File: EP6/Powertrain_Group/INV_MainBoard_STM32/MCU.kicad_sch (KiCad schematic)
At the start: 56 parts, among them J4 STDC14, SW1 RESET, U22 TCAN1042VDRQ1, U4 STM32G474RETx, U5 CAT24C256, U6 TCAN1042VDRQ1, Y1 Crystal_GND23

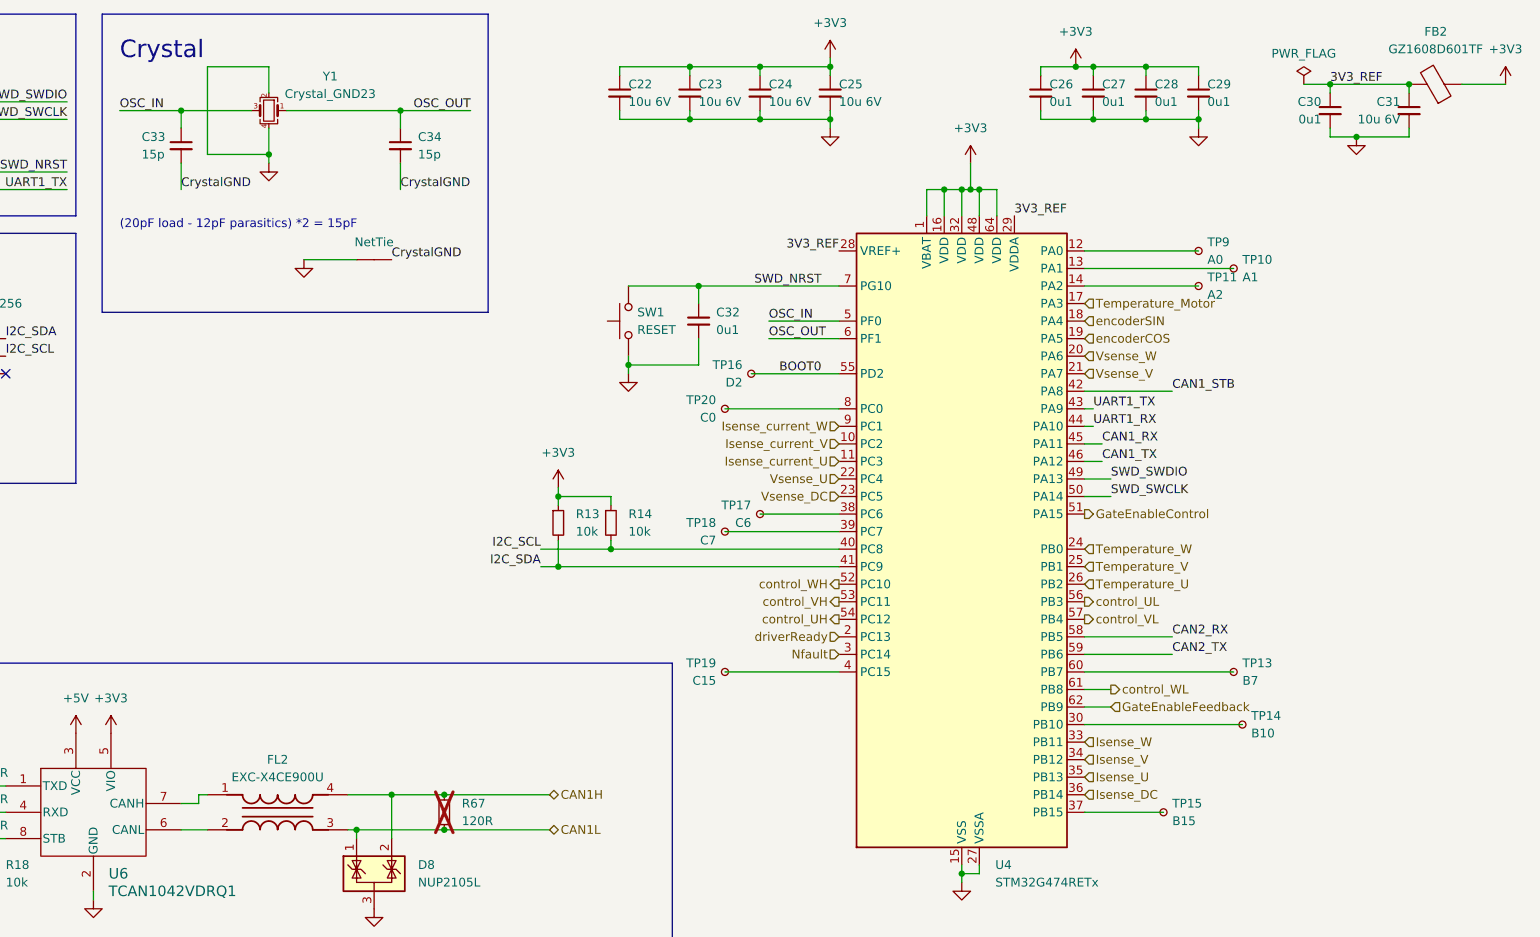
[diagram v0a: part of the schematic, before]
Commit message: batch update for JLCPCB 241117
6SBMS
ACC_HVLV1
INV_CurrentSense2
INV_CurrentSense3
DClinkCap1
INV_MainBoard_STM32
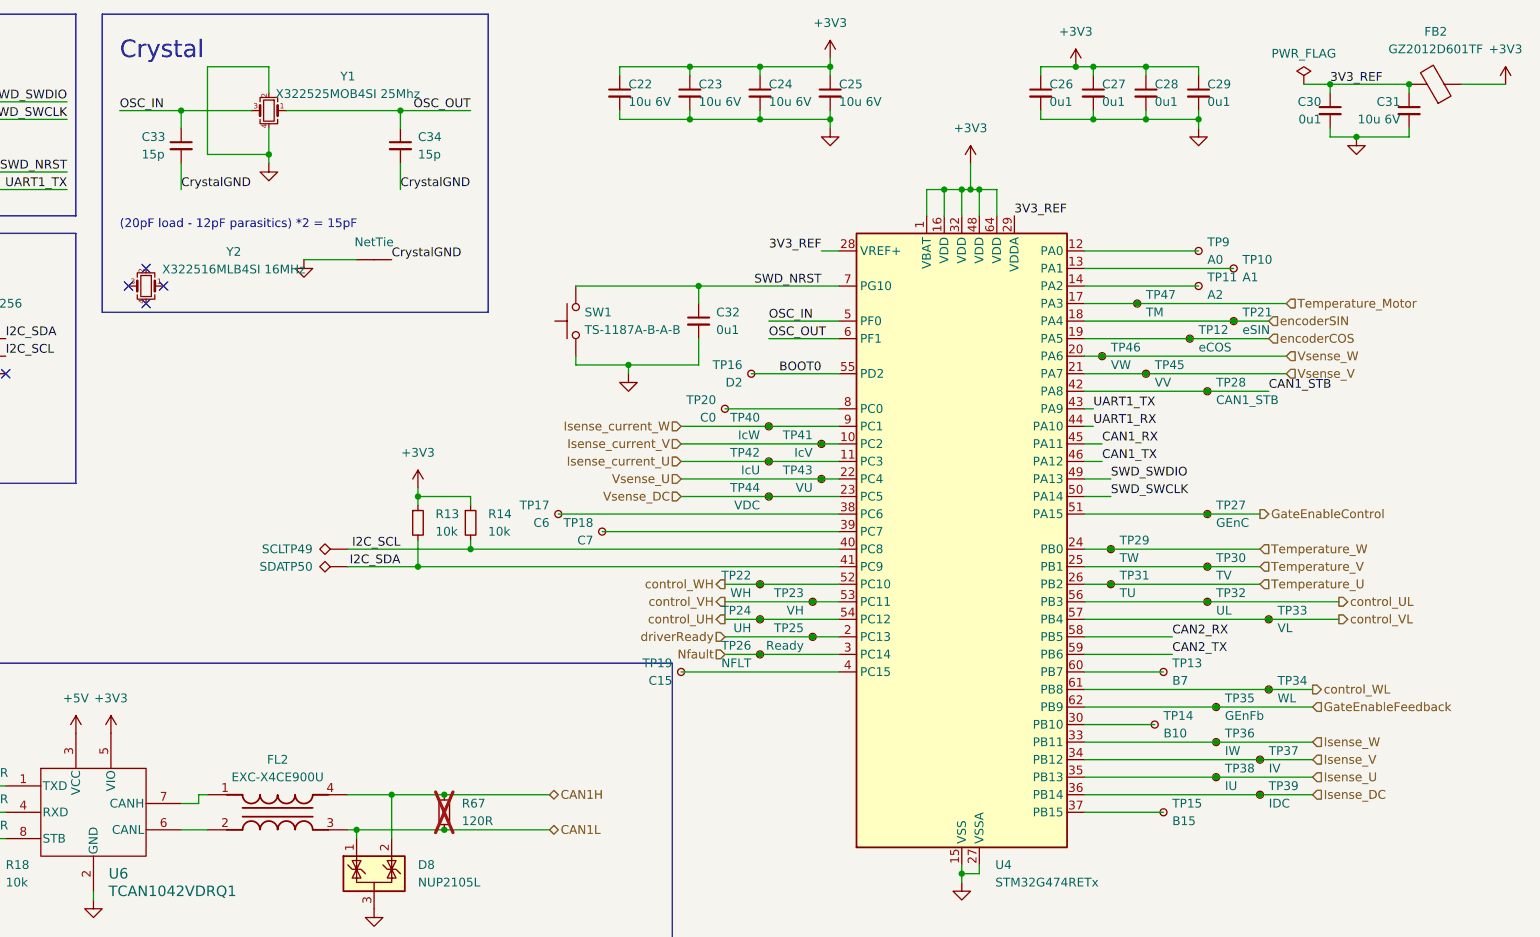
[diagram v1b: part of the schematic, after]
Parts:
- added TP12: eCOS, TestPoint:TestPoint_Pad_D1.0mm, symbol Connector:TestPoint_Small
- added TP21: eSIN, TestPoint:TestPoint_Pad_D1.0mm, symbol Connector:TestPoint_Small
- added TP22: WH, TestPoint:TestPoint_Pad_D1.0mm, symbol Connector:TestPoint_Small
- added TP23: VH, TestPoint:TestPoint_Pad_D1.0mm, symbol Connector:TestPoint_Small
- added TP24: UH, TestPoint:TestPoint_Pad_D1.0mm, symbol Connector:TestPoint_Small
- added TP25: Ready, TestPoint:TestPoint_Pad_D1.0mm, symbol Connector:TestPoint_Small
- added TP26: NFLT, TestPoint:TestPoint_Pad_D1.0mm, symbol Connector:TestPoint_Small
- added TP27: GEnC, TestPoint:TestPoint_Pad_D1.0mm, symbol Connector:TestPoint_Small
- added TP28: CAN1_STB, TestPoint:TestPoint_Pad_D1.0mm, symbol Connector:TestPoint_Small
- added TP29: TW, TestPoint:TestPoint_Pad_D1.0mm, symbol Connector:TestPoint_Small
- added TP30: TV, TestPoint:TestPoint_Pad_D1.0mm, symbol Connector:TestPoint_Small
- added TP31: TU, TestPoint:TestPoint_Pad_D1.0mm, symbol Connector:TestPoint_Small
- added TP32: UL, TestPoint:TestPoint_Pad_D1.0mm, symbol Connector:TestPoint_Small
- added TP33: VL, TestPoint:TestPoint_Pad_D1.0mm, symbol Connector:TestPoint_Small
- added TP34: WL, TestPoint:TestPoint_Pad_D1.0mm, symbol Connector:TestPoint_Small
- added TP35: GEnFb, TestPoint:TestPoint_Pad_D1.0mm, symbol Connector:TestPoint_Small
- added TP36: IW, TestPoint:TestPoint_Pad_D1.0mm, symbol Connector:TestPoint_Small
- added TP37: IV, TestPoint:TestPoint_Pad_D1.0mm, symbol Connector:TestPoint_Small
- added TP38: IU, TestPoint:TestPoint_Pad_D1.0mm, symbol Connector:TestPoint_Small
- added TP39: IDC, TestPoint:TestPoint_Pad_D1.0mm, symbol Connector:TestPoint_Small
- added TP40: IcW, TestPoint:TestPoint_Pad_D1.0mm, symbol Connector:TestPoint_Small
- added TP41: IcV, TestPoint:TestPoint_Pad_D1.0mm, symbol Connector:TestPoint_Small
- added TP42: IcU, TestPoint:TestPoint_Pad_D1.0mm, symbol Connector:TestPoint_Small
- added TP43: VU, TestPoint:TestPoint_Pad_D1.0mm, symbol Connector:TestPoint_Small
- added TP44: VDC, TestPoint:TestPoint_Pad_D1.0mm, symbol Connector:TestPoint_Small
- added TP45: VV, TestPoint:TestPoint_Pad_D1.0mm, symbol Connector:TestPoint_Small
- added TP46: VW, TestPoint:TestPoint_Pad_D1.0mm, symbol Connector:TestPoint_Small
- added TP47: TM, TestPoint:TestPoint_Pad_D1.0mm, symbol Connector:TestPoint_Small
- added TP49: SCL, TestPoint:TestPoint_THTPad_D1.0mm_Drill0.5mm, symbol Connector:TestPoint_Alt
- added TP50: SDA, TestPoint:TestPoint_THTPad_D1.0mm_Drill0.5mm, symbol Connector:TestPoint_Alt
- added Y2: X322516MLB4SI 16MHz, Crystal:Crystal_SMD_3225-4Pin_3.2x2.5mm, symbol Device:Crystal_GND24_Small
- FB2: value GZ1608D601TF -> GZ2012D601TF
- SW1: value RESET -> TS-1187A-B-A-B
- Y1: value Crystal_GND23 -> X322525MOB4SI 25Mhz
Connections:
- net CAN1_STB: now also TP28.1
- net GateEnableControl: now also TP27.1
- net GateEnableFeedback: now also TP35.1
- net I2C_SCL: now also TP49.1
- net I2C_SDA: now also TP50.1
- net Isense_DC: now also TP39.1
- net Isense_U: now also TP38.1
- net Isense_V: now also TP37.1
- net Isense_W: now also TP36.1
- net Isense_current_U: now also TP42.1
- net Isense_current_V: now also TP41.1
- net Isense_current_W: now also TP40.1
- net Nfault: now also TP26.1
- net Temperature_Motor: now also TP47.1
- net Temperature_U: now also TP31.1
- net Temperature_V: now also TP30.1
- net Temperature_W: now also TP29.1
- net Vsense_DC: now also TP44.1
- net Vsense_U: now also TP43.1
- net Vsense_V: now also TP45.1
- net Vsense_W: now also TP46.1
- net control_UH: now also TP24.1
- net control_UL: now also TP32.1
- net control_VH: now also TP23.1
- net control_VL: now also TP33.1
- net control_WH: now also TP22.1
- net control_WL: now also TP34.1
- net driverReady: now also TP25.1
- net encoderCOS: now also TP12.1
- net encoderSIN: now also TP21.1
- no-connect marks 9 -> 13
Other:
- moved on the sheet: R13, R14, SW1, TP13, TP14, TP17, TP18, TP19

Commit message: update INV_MainBoard_STM32 to V2.0
big update to match new INV_GateDriver
and use H743ZI as MCU
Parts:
- removed C18, C19, C36, C37: 0u1, Capacitor_SMD:C_0402_1005Metric, symbol Device:C_Small
- removed C35: 1u, Capacitor_SMD:C_0402_1005Metric, symbol Device:C_Small
- removed D17, D8: NUP2105L, Package_TO_SOT_SMD:SOT-23, symbol Power_Protection:NUP2105L
- removed FL2, FL3: EXC-X4CE900U, SamacSys_Parts_EP6:EXCX4CE900U, symbol SamacSys_Parts_EP6:EXC-X4CE900U
- removed J4: STDC14, nturt_kicad_lib_EP6:box_header_14P_pitch127, symbol Connector_Generic:Conn_02x07_Odd_Even
- removed JP1: CAN2STB, Jumper:SolderJumper-2_P1.3mm_Open_RoundedPad1.0x1.5mm, symbol Jumper:SolderJumper_2_Open
- removed R12: 100R, Resistor_SMD:R_0603_1608Metric, symbol Device:R_Small
- removed R15, R16, R17, R70, R71, R73: 100R, Resistor_SMD:R_0402_1005Metric, symbol Device:R_Small
- removed R67, R72: 120R, Resistor_SMD:R_0402_1005Metric, symbol Device:R_Small
- removed R74: 10k, Resistor_SMD:R_0402_1005Metric, symbol Device:R_Small
- removed TIE2: NetTie, NetTie:NetTie-2_SMD_Pad0.5mm, symbol PCM_4ms_Net-tie:NetTie
- removed TP10: A1, TestPoint:TestPoint_Pad_D1.0mm, symbol Connector:TestPoint_Small
- removed TP11: A2, TestPoint:TestPoint_Pad_D1.0mm, symbol Connector:TestPoint_Small
- removed TP12: eCOS, TestPoint:TestPoint_Pad_D1.0mm, symbol Connector:TestPoint_Small
- removed TP13: B7, TestPoint:TestPoint_Pad_D1.0mm, symbol Connector:TestPoint_Small
- removed TP14: B10, TestPoint:TestPoint_Pad_D1.0mm, symbol Connector:TestPoint_Small
- removed TP15: B15, TestPoint:TestPoint_Pad_D1.0mm, symbol Connector:TestPoint_Small
- removed TP16: D2, TestPoint:TestPoint_Pad_D1.0mm, symbol Connector:TestPoint_Small
- removed TP17: C6, TestPoint:TestPoint_Pad_D1.0mm, symbol Connector:TestPoint_Small
- removed TP18: C7, TestPoint:TestPoint_Pad_D1.0mm, symbol Connector:TestPoint_Small
- removed TP19: C15, TestPoint:TestPoint_Pad_D1.0mm, symbol Connector:TestPoint_Small
- removed TP20: C0, TestPoint:TestPoint_Pad_D1.0mm, symbol Connector:TestPoint_Small
- removed TP21: eSIN, TestPoint:TestPoint_Pad_D1.0mm, symbol Connector:TestPoint_Small
- removed TP22: WH, TestPoint:TestPoint_Pad_D1.0mm, symbol Connector:TestPoint_Small
- removed TP23: VH, TestPoint:TestPoint_Pad_D1.0mm, symbol Connector:TestPoint_Small
- removed TP24: UH, TestPoint:TestPoint_Pad_D1.0mm, symbol Connector:TestPoint_Small
- removed TP25: Ready, TestPoint:TestPoint_Pad_D1.0mm, symbol Connector:TestPoint_Small
- removed TP26: NFLT, TestPoint:TestPoint_Pad_D1.0mm, symbol Connector:TestPoint_Small
- removed TP27: GEnC, TestPoint:TestPoint_Pad_D1.0mm, symbol Connector:TestPoint_Small
- removed TP28: CAN1_STB, TestPoint:TestPoint_Pad_D1.0mm, symbol Connector:TestPoint_Small
- removed TP29: TW, TestPoint:TestPoint_Pad_D1.0mm, symbol Connector:TestPoint_Small
- removed TP30: TV, TestPoint:TestPoint_Pad_D1.0mm, symbol Connector:TestPoint_Small
- removed TP31: TU, TestPoint:TestPoint_Pad_D1.0mm, symbol Connector:TestPoint_Small
- removed TP32: UL, TestPoint:TestPoint_Pad_D1.0mm, symbol Connector:TestPoint_Small
- removed TP33: VL, TestPoint:TestPoint_Pad_D1.0mm, symbol Connector:TestPoint_Small
- removed TP34: WL, TestPoint:TestPoint_Pad_D1.0mm, symbol Connector:TestPoint_Small
- removed TP35: GEnFb, TestPoint:TestPoint_Pad_D1.0mm, symbol Connector:TestPoint_Small
- removed TP36: IW, TestPoint:TestPoint_Pad_D1.0mm, symbol Connector:TestPoint_Small
- removed TP37: IV, TestPoint:TestPoint_Pad_D1.0mm, symbol Connector:TestPoint_Small
- removed TP38: IU, TestPoint:TestPoint_Pad_D1.0mm, symbol Connector:TestPoint_Small
- removed TP39: IDC, TestPoint:TestPoint_Pad_D1.0mm, symbol Connector:TestPoint_Small
- removed TP40: IcW, TestPoint:TestPoint_Pad_D1.0mm, symbol Connector:TestPoint_Small
- removed TP41: IcV, TestPoint:TestPoint_Pad_D1.0mm, symbol Connector:TestPoint_Small
- removed TP42: IcU, TestPoint:TestPoint_Pad_D1.0mm, symbol Connector:TestPoint_Small
- removed TP43: VU, TestPoint:TestPoint_Pad_D1.0mm, symbol Connector:TestPoint_Small
- removed TP44: VDC, TestPoint:TestPoint_Pad_D1.0mm, symbol Connector:TestPoint_Small
- removed TP45: VV, TestPoint:TestPoint_Pad_D1.0mm, symbol Connector:TestPoint_Small
- removed TP46: VW, TestPoint:TestPoint_Pad_D1.0mm, symbol Connector:TestPoint_Small
- removed TP47: TM, TestPoint:TestPoint_Pad_D1.0mm, symbol Connector:TestPoint_Small
- removed TP49: SCL, TestPoint:TestPoint_THTPad_D1.0mm_Drill0.5mm, symbol Connector:TestPoint_Alt
- removed TP50: SDA, TestPoint:TestPoint_THTPad_D1.0mm_Drill0.5mm, symbol Connector:TestPoint_Alt
- removed TP9: A0, TestPoint:TestPoint_Pad_D1.0mm, symbol Connector:TestPoint_Small
- removed U22, U6: TCAN1042VDRQ1, Package_SO:SOIC-8_3.9x4.9mm_P1.27mm, symbol nturt_kicad_lib_EP6:TCAN1042VDRQ1
- removed U4: STM32G474RETx, Package_QFP:LQFP-64_10x10mm_P0.5mm, symbol MCU_ST_STM32G4:STM32G474RETx
- removed U5: CAT24C256, Package_SO:SOIC-8_3.9x4.9mm_P1.27mm, symbol Memory_EEPROM:CAT24C256
- removed Y1: X322525MOB4SI 25Mhz, Crystal:Crystal_SMD_3225-4Pin_3.2x2.5mm, symbol Device:Crystal_GND24_Small
- removed Y2: X322516MLB4SI 16MHz, Crystal:Crystal_SMD_3225-4Pin_3.2x2.5mm, symbol Device:Crystal_GND24_Small
- added BT1: 1056, nturt_kicad_lib_EP6:BAT_1056, symbol nturt_kicad_lib_EP6:1056
- added C39, C50, C53, C64: 0u1, Capacitor_SMD:C_0402_1005Metric, symbol Device:C_Small
- added C44, C45: 2u2, Capacitor_SMD:C_0402_1005Metric, symbol Device:C_Small
- added C51, C60, C61, C62, C63: 100n, Capacitor_SMD:C_0402_1005Metric, symbol Device:C_Small
- added C55, C56, C67: 4u7, Capacitor_SMD:C_0402_1005Metric, symbol Device:C_Small
- added C65, C66: 10u 6V, Capacitor_SMD:C_0402_1005Metric, symbol Device:C_Small
- added C87, C88: 22u, Capacitor_SMD:C_0805_2012Metric, symbol Device:C_Small
- added C91, C92: 470n, Capacitor_SMD:C_0603_1608Metric, symbol Device:C_Small
- added D10, D22: G LED, LED_SMD:LED_0603_1608Metric, symbol Device:LED_Small_Filled
- added D11, D18, D20: R LED, LED_SMD:LED_0603_1608Metric, symbol Device:LED_Small_Filled
- added D13, D23: B LED, LED_SMD:LED_0603_1608Metric, symbol Device:LED_Small_Filled
- added D14, D21: Y LED, LED_SMD:LED_0603_1608Metric, symbol Device:LED_Small_Filled
- added D16: W LED, LED_SMD:LED_0603_1608Metric, symbol Device:LED_Small_Filled
- added J15: STDC14, nturt_kicad_lib_EP6:box_header_14P_pitch127, symbol Connector_Generic:Conn_02x07_Odd_Even
- added J4: MSD-4-A, MSD4A, symbol SamacSys_Parts_EP6:MSD-4-A
- added R12, R24, R42, R46, R62: 4k7, Resistor_SMD:R_0402_1005Metric, symbol Device:R
- added R66, R73: 10k, Resistor_SMD:R_0402_1005Metric, symbol Device:R
- added R68, R77, R78, R80, R86, R87, R88: 2k2, Resistor_SMD:R_0402_1005Metric, symbol Device:R_Small
- added R69: 10k, Resistor_SMD:R_0402_1005Metric, symbol Device:R_Small
- added R75: 100R, Resistor_SMD:R_0402_1005Metric, symbol Device:R_Small
- added SW2, SW3: TS-1187A-B-A-B, Button_Switch_SMD:SW_SPST_TL3342, symbol Switch:SW_Push
- added U1: STM32H743ZITx, Package_QFP:LQFP-144_20x20mm_P0.5mm, symbol MCU_ST_STM32H7:STM32H743ZITx
- added U23: REF3133AQDBZRQ1, Package_TO_SOT_SMD:SOT-23, symbol PCM_Voltage_Regulator_AKL:Regulator_Generic_IN_OUT_GND
- added Y1: 48MHz YF4048M00033T8188103, Crystal:Crystal_SMD_3225-4Pin_3.2x2.5mm, symbol Device:Crystal_GND24
- added Y2: 32.768kHz Q13FC13500004, Crystal:Crystal_SMD_3215-2Pin_3.2x1.5mm, symbol Device:Crystal
- C22, C23, C24, C25: value 10u 6V -> 100n
- C26, C27, C29: value 0u1 -> 100n
- C28: value 0u1 -> 4u7
- C30: value 0u1 -> 15p
- C31: value 10u 6V -> 15p
- C33, C34: value 15p -> 27p
- FB2: value GZ2012D601TF -> GZ1608D601TF; footprint Inductor_SMD:L_0805_2012Metric -> Capacitor_SMD:C_0603_1608Metric
- R13, R14, R18: value 10k -> 2k2
- SW1: footprint Button_Switch_SMD:SW_Push_1P1T_XKB_TS-1187A -> Button_Switch_SMD:SW_SPST_TL3342
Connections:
- net CrystalGND is gone; now on net GND: C33.2, C34.2
- net +3V3: now also FB2.2, C51.1, C55.1, C56.1, C60.1, C61.1, C62.1, C63.1, C66.1, C67.1, J15.3 (Pin_3), J4.4 (VDD), R12.2, R24.2, R42.2, R46.2, R62.2, R66.1, R69.1, U1.108 (VDD), U1.121 (VDD), U1.131 (VDD), U1.144 (VDD), U1.17 (VDD), U1.30 (VDD), U1.39 (VDD), U1.52 (VDD), U1.62 (VDD), U1.72 (VDD), U1.84 (VDD), U1.95 (VDD33_USB); no longer FB2.1, R13.1, R14.1
- net +5V: now also C92.1, U23.1 (IN)
- net CAN1_RX: now also U1.139 (PB8)
- net CAN1_TX: now also U1.140 (PB9)
- net CAN2_RX: now also U1.135 (PB5)
- net CAN2_TX: now also U1.136 (PB6)
- net GND: now also BT1.N, C39.2, C44.2, C45.2, C50.2, C51.2, C53.2, C55.2, C56.2, C60.2, C61.2, C62.2, C63.2, C64.2, C65.2, C66.2, C67.2, C87.2, C88.2, C91.2, C92.2, D10.1 (K), D11.1 (K), D13.1 (K), D14.1 (K), D16.1 (K), D18.1 (K), D20.1 (K), D21.1 (K), D22.1 (K), D23.1 (K), J15.5 (Pin_5), J15.7 (Pin_7), J4.6 (VSS), J4.G1 (GND_1), J4.G2 (GND_2), J4.G3 (GND_3), J4.G4 (GND_4), R73.1, R75.1, SW2.1, SW3.1, U1.107 (VSS), U1.120 (VSS), U1.130 (VSS), U1.16 (VSS), U1.31 (VSSA), U1.38 (VSS), U1.51 (VSS), U1.61 (VSS), U1.83 (VSS), U1.94 (VSS), U23.3, Y1.2, Y1.4; no longer R18.2
- net GateEnableControl: now also U1.119 (PD5)
- net GateEnableFeedback: now also U1.122 (PD6)
- net Isense_DC: now also U1.47 (PB1)
- net Isense_U: now also U1.46 (PB0)
- net Isense_V: now also U1.45 (PC5)
- net Isense_W: now also U1.44 (PC4)
- net OSC_IN: now also C34.1, U1.23 (PH0), Y1.3; no longer C33.1
- net OSC_OUT: now also C33.1, U1.24 (PH1), Y1.1; no longer C34.1
- net Temperature_Motor: now also U1.21 (PF9)
- net Temperature_U: now also U1.18 (PF6)
- net Temperature_V: now also U1.19 (PF7)
- net Temperature_W: now also U1.20 (PF8)
- net Vsense_DC: now also U1.28 (PC2_C)
- net control_UH: now also U1.60 (PE9)
- net control_UL: now also U1.59 (PE8)
- net control_VH: now also U1.64 (PE11)
- net control_VL: now also U1.63 (PE10)
- net control_WH: now also U1.66 (PE13)
- net control_WL: now also U1.65 (PE12)
- net driverReady: now also U1.115 (PD1)
- net LED_D13: now reaches R18.1
- net LED_D13: now also U1.82 (PD13)
- removed net 3V3_REF: C30.1, C31.1, FB2.2
- net I2C_SCL: no longer names the net of R14.2
- net I2C_SCL: now also D16.2 (A)
- net I2C_SDA: no longer names the net of R13.2
- net I2C_SDA: now also D13.2 (A)
- net SWD_NRST renamed NRST
- net NRST: now also C50.1, J15.12 (Pin_12), R69.2, U1.25 (NRST)
- new net: D23.2 (A), R88.2
- new net: D20.2 (A), R80.2
- new net: D22.2 (A), R87.2
- new net: J15.11 (Pin_11), R75.2
- new net: R73.2, U1.138 (BOOT0)
- new net: R66.2, U1.143 (PDR_ON)
- new net: D18.2 (A), R18.2
- new net: D10.2 (A), R78.2
- new net: D14.2 (A), R68.2
- new net: D11.2 (A), R77.2
- new net: D21.2 (A), R86.2
- new net BUT_G2: C53.1, SW3.2, U1.87 (PG2)
- new net BUT_G3: C39.1, SW2.2, U1.88 (PG3)
- new net COS+: U1.42 (PA6)
- new net COS-: U1.43 (PA7)
- new net GateNfault: U1.117 (PD3)
- new net I2C2_SCL: U1.11 (PF1)
- new net I2C2_SDA: U1.10 (PF0)
- new net LED_B12: R80.1, U1.73 (PB12)
- new net LED_B13: R86.1, U1.74 (PB13)
- new net LED_B14: R87.1, U1.75 (PB14)
- new net LED_B15: R88.1, U1.76 (PB15)
- new net LED_D10: R78.1, U1.79 (PD10)
- new net LED_D11: R13.1, U1.80 (PD11)
- new net LED_D12: R14.1, U1.81 (PD12)
- new net LED_D8: R77.1, U1.77 (PD8)
- new net LED_D9: R68.1, U1.78 (PD9)
- new net OCPNfault: U1.118 (PD4)
- new net OSC32_IN: C31.1, U1.8 (PC14), Y2.2
- new net OSC32_OUT: C30.1, U1.9 (PC15), Y2.1
- new net SDMMC1_CK: J4.5 (CLK), U1.113 (PC12)
- new net SDMMC1_CMD: J4.3 (CMD), R62.1, U1.116 (PD2)
- new net SDMMC1_D0: J4.7 (DAT0), R12.1, U1.98 (PC8)
- new net SDMMC1_D1: J4.8 (DAT1), R24.1, U1.99 (PC9)
- new net SDMMC1_D2: J4.1 (DAT2), R42.1, U1.111 (PC10)
- new net SDMMC1_D3: J4.2 (CD/DAT3), R46.1, U1.112 (PC11)
- new net SIN+: U1.40 (PA4)
- new net SIN-: U1.41 (PA5)
- new net SPI4_CS1: U1.2 (PE3)
- new net SPI4_CS2: U1.3 (PE4)
- new net SPI4_MISO: U1.4 (PE5)
- new net SPI4_MOSI: U1.5 (PE6)
- new net SPI4_SCK: U1.1 (PE2)
- new net T_CLK: J15.6 (Pin_6), U1.109 (PA14)
- new net T_DIO: J15.4 (Pin_4), U1.105 (PA13)
- new net USART1_RX: J15.13 (Pin_13), U1.102 (PA10)
- new net USART1_TX: J15.14 (Pin_14), U1.101 (PA9)
- new net VBAT: BT1.P, U1.6 (VBAT)
- new net VCAP1: C44.1, U1.71 (VCAP)
- new net VCAP2: C45.1, U1.106 (VCAP)
- new net VDDA_MCU: C64.1, C65.1, FB2.1, U1.33 (VDDA)
- new net VDDA_REF: C87.1, C88.1, C91.1, U1.32 (VREF+), U23.2 (OUT)
- new net lowVoltDetect: U1.90 (PG5)
- no-connect marks 13 -> 58
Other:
- note added: "NC"
- note added: "SDMMC"
- note added: "STDC14 to stlink"
- note added: "SWO"
- note added: "T_RX"
- note added: "T_TX"
- note added: "currently different from IOC UVW sequence is same but the HL are reversed"
- note added: "load capacitance : 15pF"
- note added: "reference: 32F746GDISCOVERY"
- note removed: "(20pF load - 12pF parasitics) *2 = 15pF"
- note removed: "Address inputs and WP has on-chip pull-down resistors"
- note removed: "CAN1"
- note removed: "Crystal"
- note removed: "EEPROM"
- note removed: "SWD"
- title: INV_MainBoard -> INV_MainBoard_STM32
- moved on the sheet: C32, C33, C34, SW1

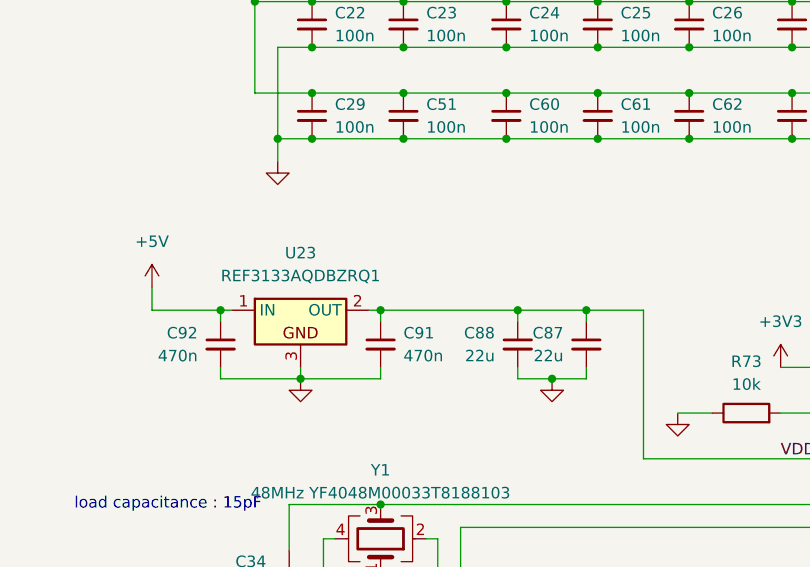
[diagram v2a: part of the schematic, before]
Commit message: update INV_MainBoard_STM32 to V2.1
update for JLCPCB, include change in 1.65 Vref and some name change for easier JLCPCBA BOM selection
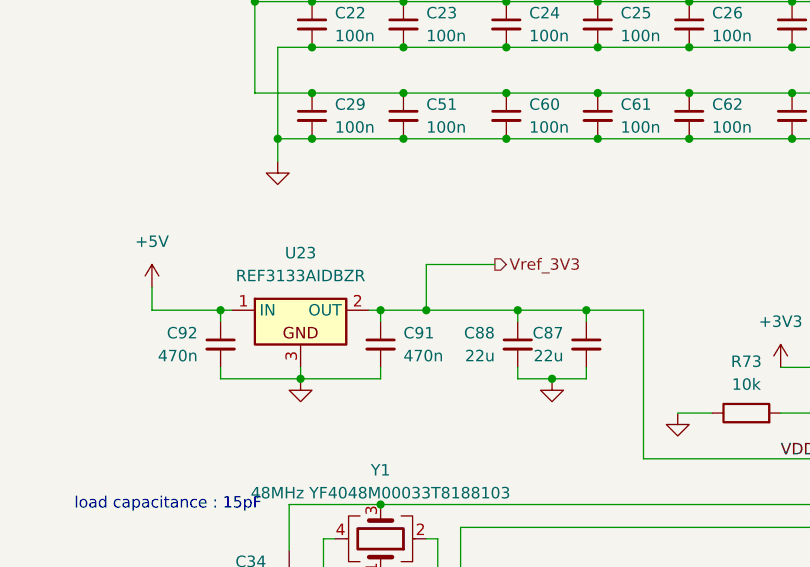
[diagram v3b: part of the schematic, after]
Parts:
- U23: value REF3133AQDBZRQ1 -> REF3133AIDBZR
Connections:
- net VDDA_REF renamed Vref_3V3
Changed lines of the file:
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@@
 		(title "INV_MainBoard_STM32")
 		(date "2025-02-28")
-		(rev "2.0")
+		(rev "2.1")
 		(company "NTURacing Team")
 		(comment 1 "郭哲明 Jack Kuo")
@@
 	)
 	(junction
+		(at 114.3 74.93)
+		(diameter 0)
+		(color 0 0 0 0)
+	)
+	(junction
 		(at 109.22 113.03)
 		(diameter 0)
@@
 	(wire
 		(pts
+			(xy 121.92 69.85) (xy 114.3 69.85)
+		)
+		(stroke
+			(width 0)
+			(type default)
+		)
+	)
+	(wire
+		(pts
 			(xy 143.51 40.64) (xy 154.94 40.64)
 		)
@@
 	(wire
 		(pts
-			(xy 109.22 74.93) (xy 124.46 74.93)
+			(xy 109.22 74.93) (xy 114.3 74.93)
 		)
 		(stroke
@@
 	(wire
 		(pts
+			(xy 114.3 69.85) (xy 114.3 74.93)
+		)
+		(stroke
+			(width 0)
+			(type default)
+		)
+	)
+	(wire
+		(pts
 			(xy 259.08 212.09) (xy 269.24 212.09)
 		)
@@
 	(wire
 		(pts
+			(xy 114.3 74.93) (xy 124.46 74.93)
+		)
+		(stroke
+			(width 0)
+			(type default)
+		)
+	)
+	(wire
+		(pts
 			(xy 95.25 39.37) (xy 95.25 40.64)
 		)
@@
 		)
 	)
+	(hierarchical_label "Vref_3V3"
+		(shape output)
+		(at 121.92 69.85 0)
+		(effects
+			(font
+				(size 1.27 1.27)
+			)
+			(justify left)
+		)
+	)
 	(hierarchical_label "Isense_W"
 		(shape input)
@@
 			)
 		)
-		(property "Value" "REF3133AQDBZRQ1"
+		(property "Value" "REF3133AIDBZR"
 			(at 100.33 71.12 0)
 			(effects

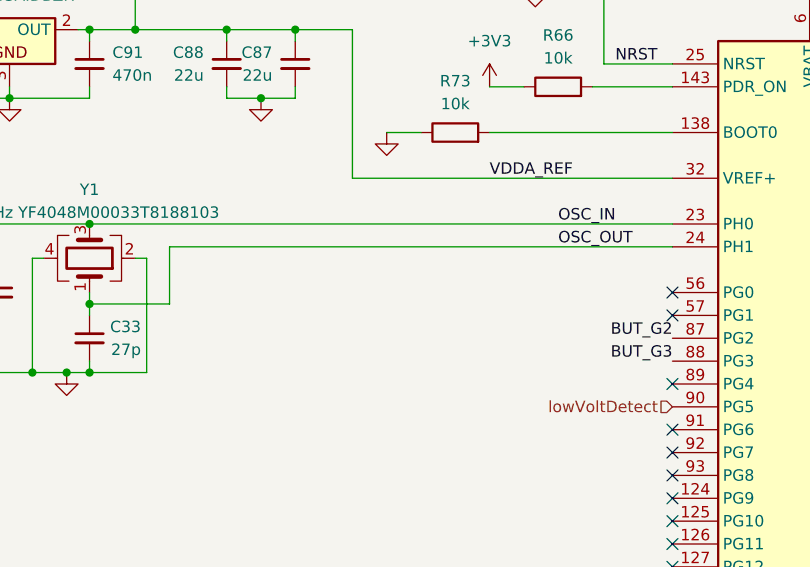
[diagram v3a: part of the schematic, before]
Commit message: add comments to INV boards after testing JLC PCBs
INV boards included:
INV_GateDriver: mainly about QSPI SPRAM
INV_MainBoard_STM32: mainly about mistake VINC of LM26420
INV_MainBoard_TI: mainly about trace too long and incorrect spec of Rg
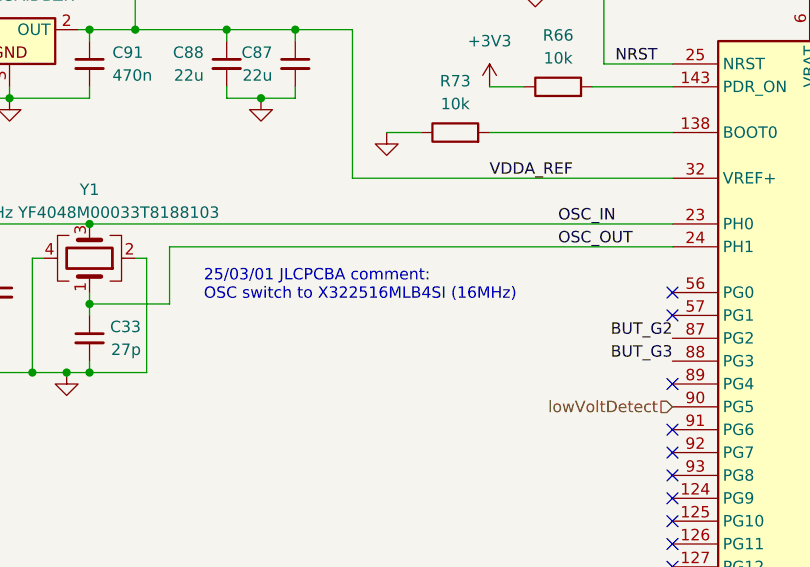
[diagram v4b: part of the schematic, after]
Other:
- note added: "25/03/01 JLCPCBA comment: OSC switch to X322516MLB4SI (16MHz)"
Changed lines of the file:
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@@
+		)
+	)
+	(text "25/03/01 JLCPCBA comment:\nOSC switch to X322516MLB4SI (16MHz)\n"
+		(exclude_from_sim no)
+		(at 121.92 101.6 0)
+		(effects
+			(font
+				(size 1.27 1.27)
+				(color 255 0 0 1)
+			)
+			(justify left top)
 		)
 	)
